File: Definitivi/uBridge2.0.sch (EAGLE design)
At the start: 43 parts, among them IC4 AP6503SP-13

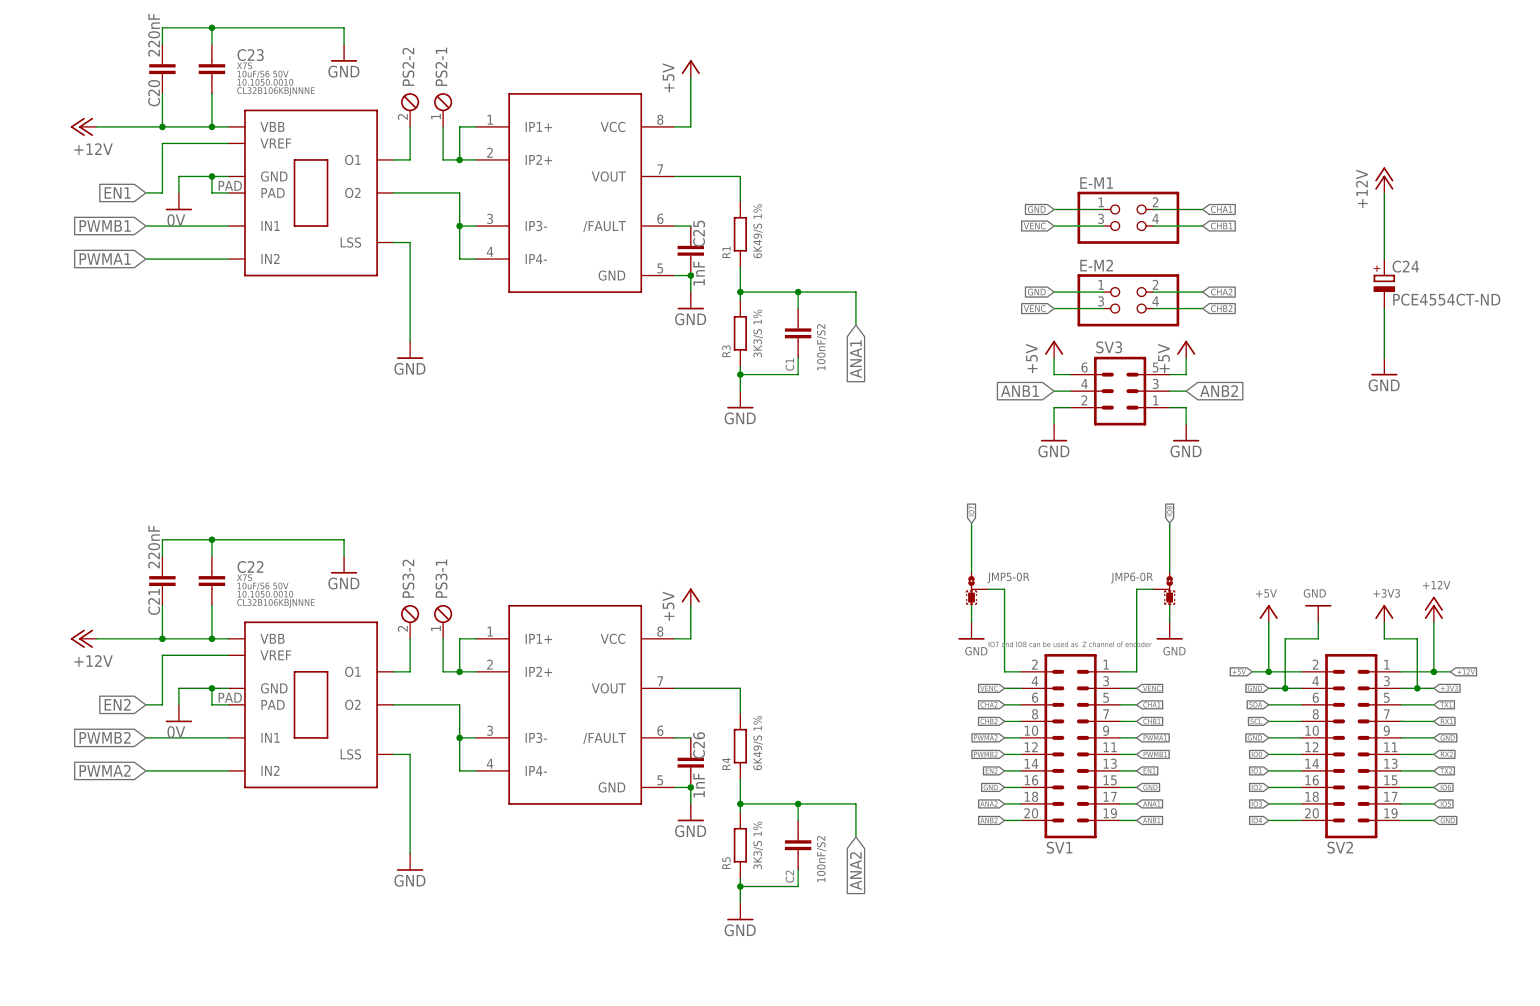
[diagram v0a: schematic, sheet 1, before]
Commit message: add SATA connector
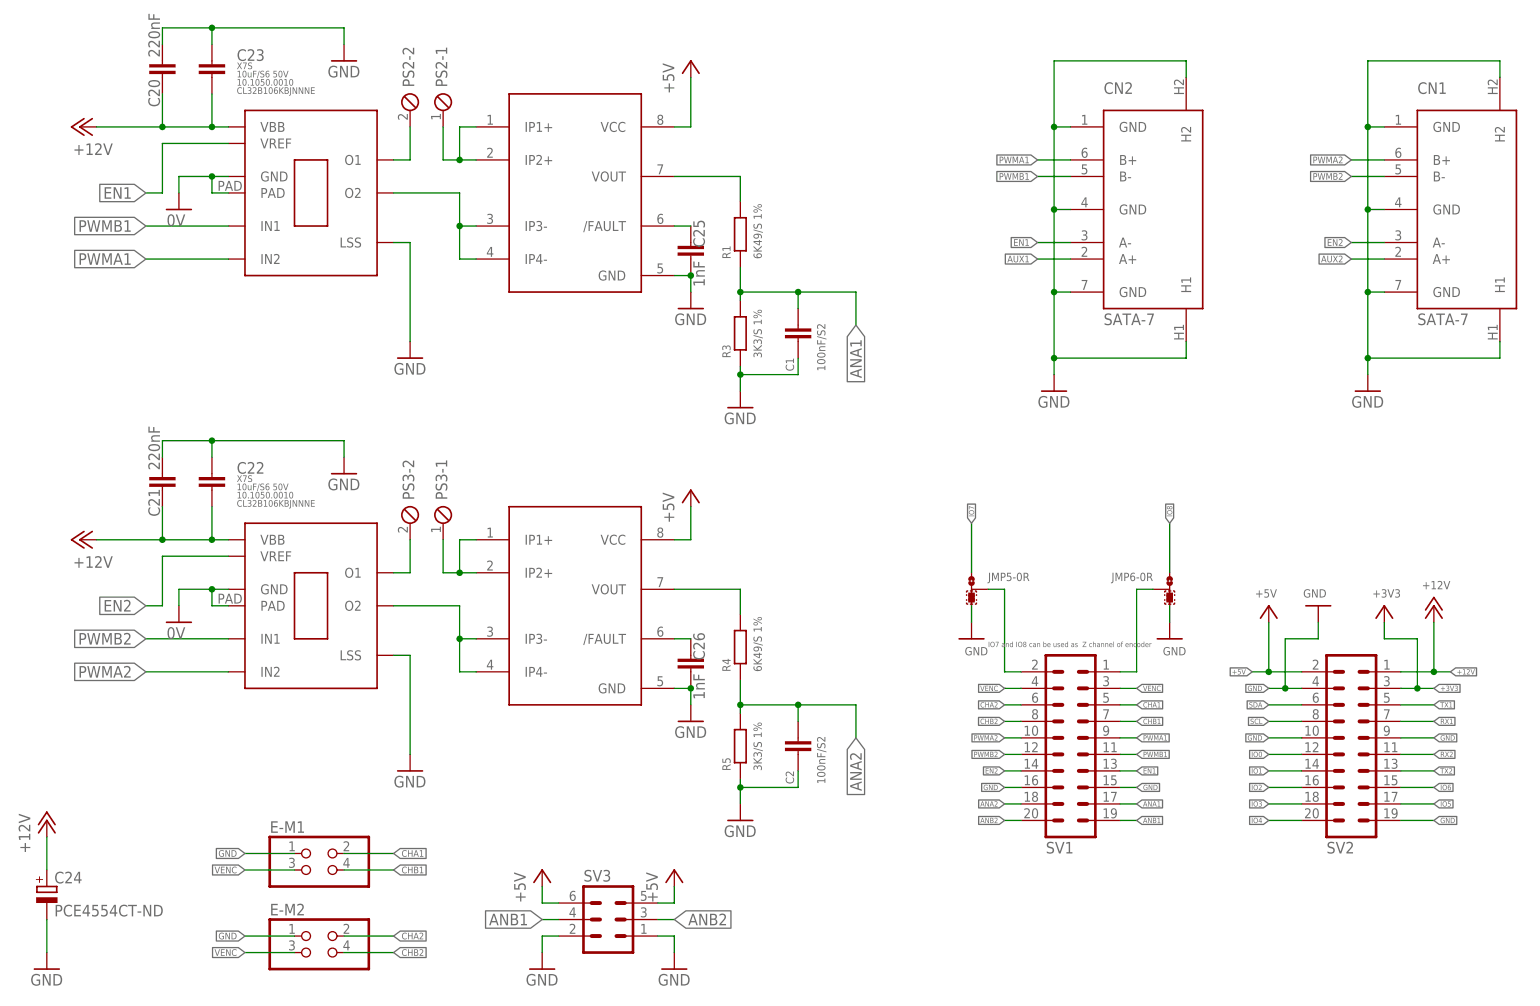
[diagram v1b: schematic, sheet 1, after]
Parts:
- added CN1, CN2: SATA-7, OfficineRobotiche:SATA-7
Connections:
- new net AUX1: CN2.A+
- new net AUX2: CN1.A+
- net EN1: now also CN2.A-
- net EN2: now also CN1.A-
- net GND: now also CN1.GND@1, CN1.GND@2, CN1.GND@3, CN1.H1, CN1.H2, CN2.GND@1, CN2.GND@2, CN2.GND@3, CN2.H1, CN2.H2
- net PWMA1: now also CN2.B+
- net PWMA2: now also CN1.B+
- net PWMB1: now also CN2.B-
- net PWMB2: now also CN1.B-
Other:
- moved on the sheet: C2, C21, C22, C24, C26, E-M1, E-M2, PS3-1, PS3-2, R4, R5, SV3
